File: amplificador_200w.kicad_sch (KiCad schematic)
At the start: 36 parts, among them Q10 A733, Q11 A733, Q12 2SC2229, Q13 2SC2229, Q14 BD139, Q15 BD136, Q16 BD139, Q17 2SC5200, Q18 2SC5200

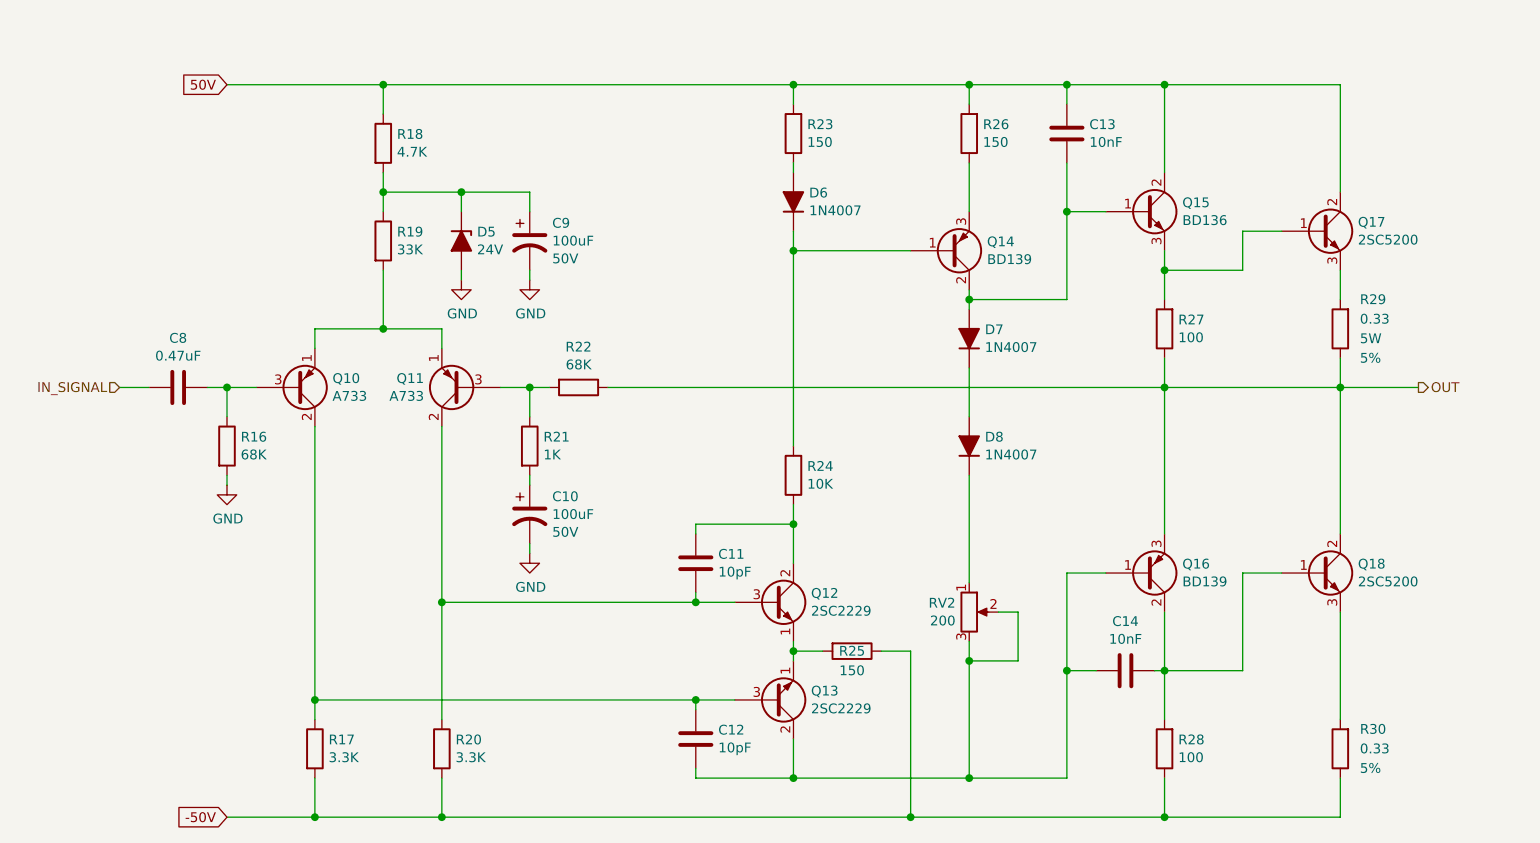
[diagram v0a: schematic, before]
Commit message: Separando las altas con resistencias de 22K
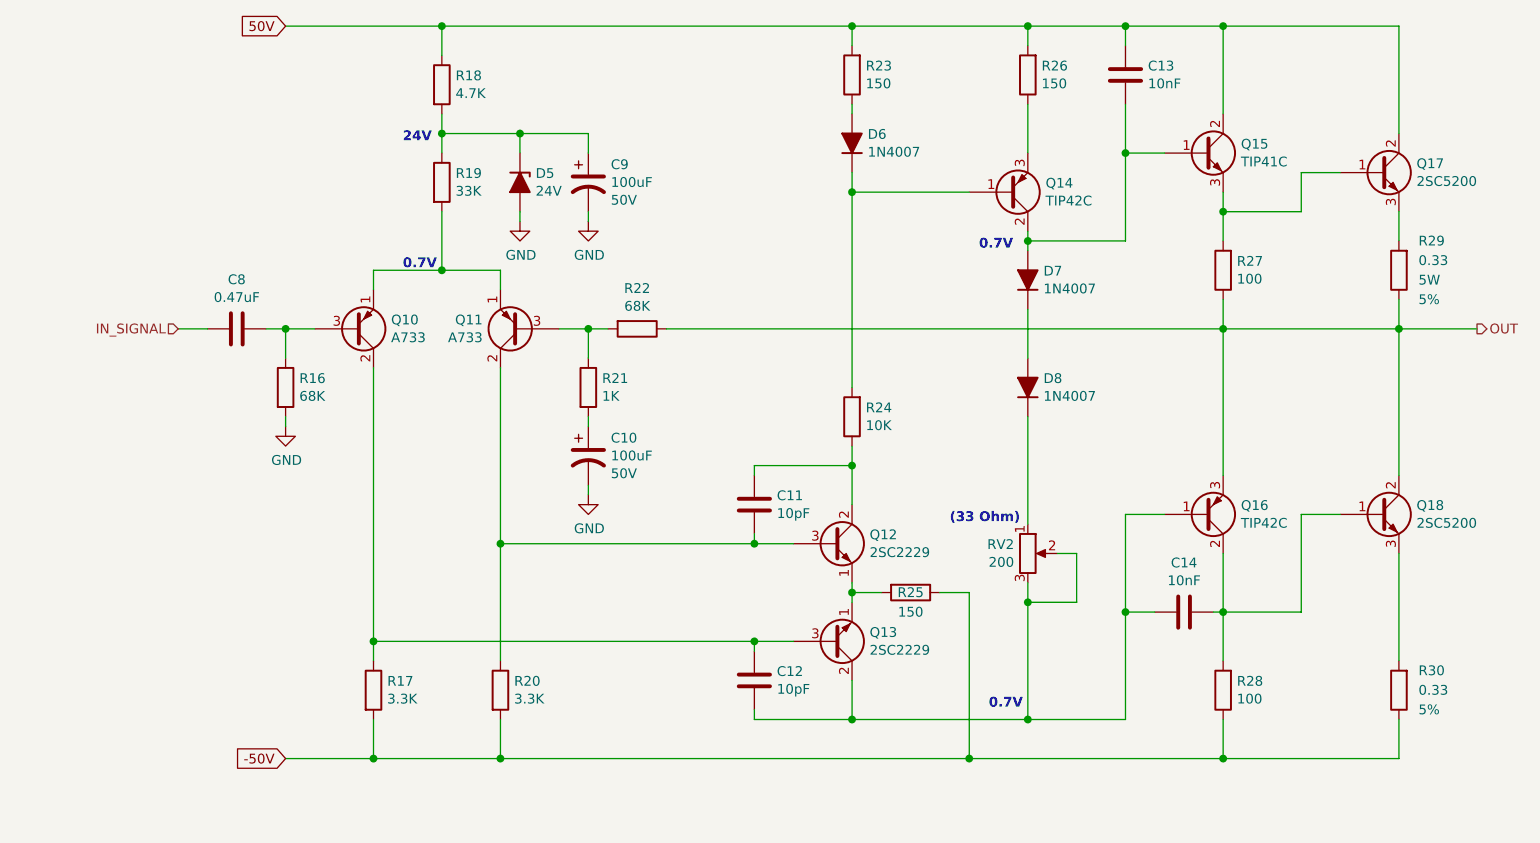
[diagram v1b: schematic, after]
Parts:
- Q14, Q16: value BD139 -> TIP42C; footprint Package_TO_SOT_THT:TO-126-3_Vertical -> Package_TO_SOT_THT:TO-220-3_Vertical
- Q15: value BD136 -> TIP41C; footprint Package_TO_SOT_THT:TO-126-3_Vertical -> Package_TO_SOT_THT:TO-220-3_Vertical
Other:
- note added: "(33 Ohm)"
- note added: "0.7V"
- note added: "24V"
- moved on the sheet: C10, C11, C12, C13, C14, C8, C9, D5, D6, D7, D8, Q10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

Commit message: actualizando a kicad 7
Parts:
- renumbered C8 to C1, C9 to C2, C10 to C3, C11 to C4, C12 to C5, C13 to C6, C14 to C7, D5 to D1, D6 to D2, D7 to D3, D8 to D4, Q10 to Q1, Q11 to Q2, Q12 to Q3, Q13 to Q4, Q14 to Q5, Q15 to Q6, Q16 to Q7, Q17 to Q8, Q18 to Q9, R16 to R1, R25 to R10, R26 to R11, R27 to R12, R28 to R13, R29 to R14, R30 to R15, R17 to R2, R18 to R3, R19 to R4, R20 to R5, R21 to R6, R22 to R7, R23 to R8, R24 to R9, RV2 to RV1
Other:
- title: Amplificador Zener 100W -> AMPLIFICADOR ESTEREO 200, CONTROL DE TONOS
